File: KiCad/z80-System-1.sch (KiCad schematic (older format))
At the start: 6 parts, among them J1 FTDI Header, U1 62256, U2 Z80CPU, U3 AT28C64, U4 16550, X1 ACO-1.8432MHz

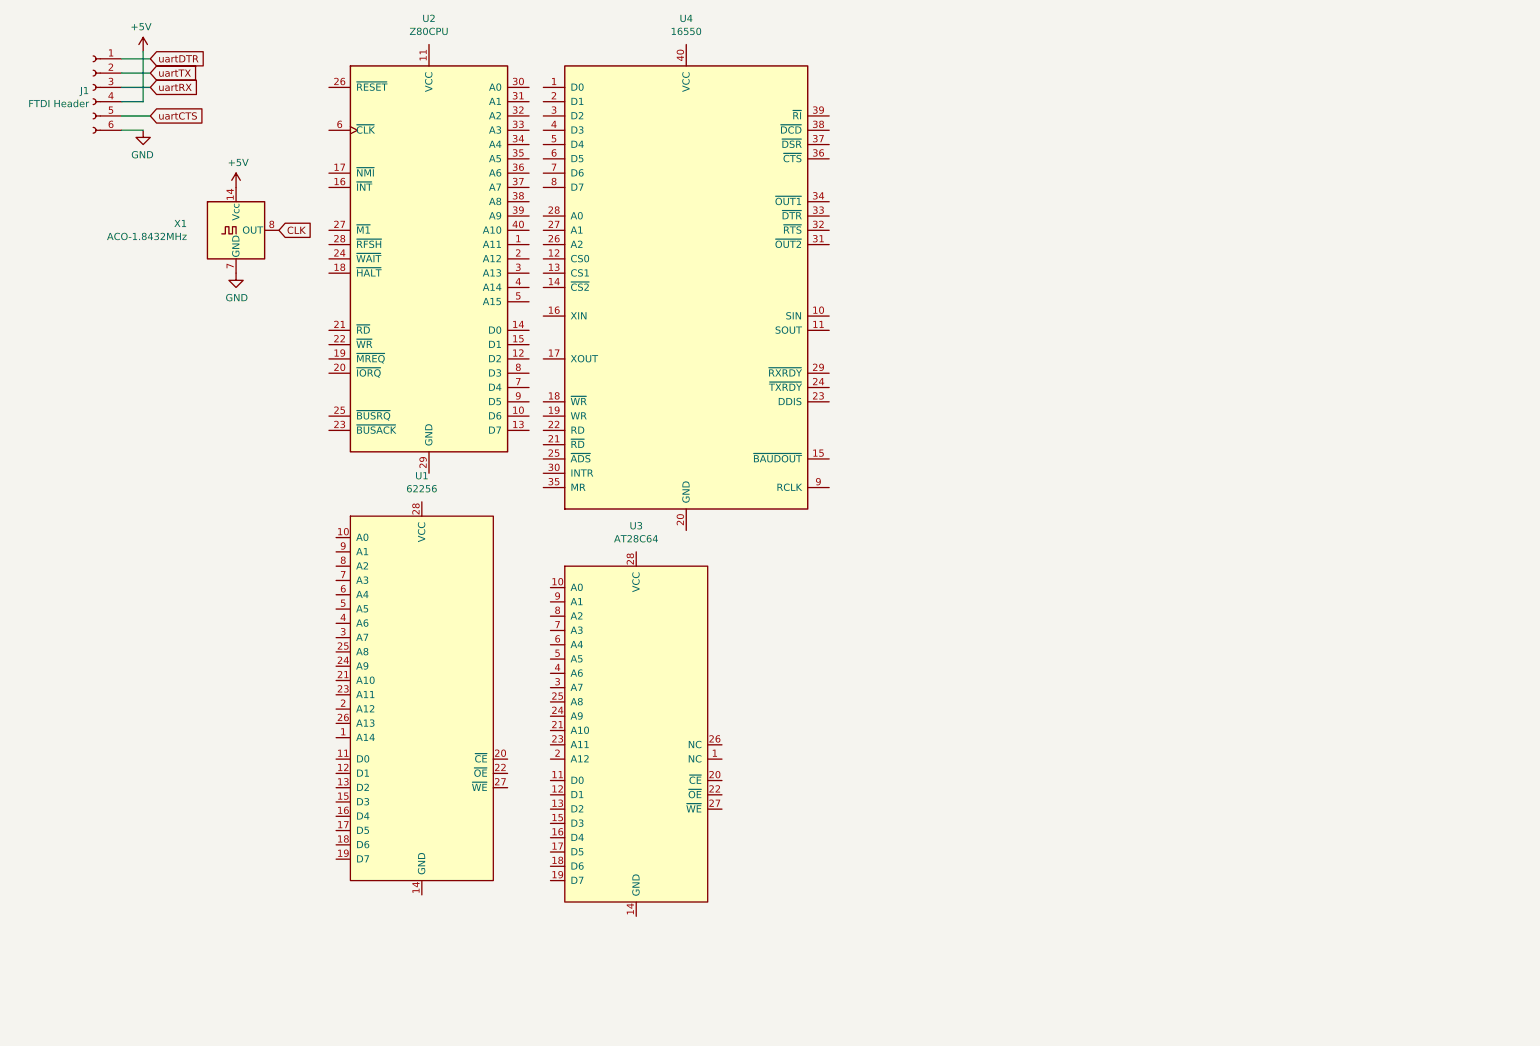
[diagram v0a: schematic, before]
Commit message: basic wiring to the cpu
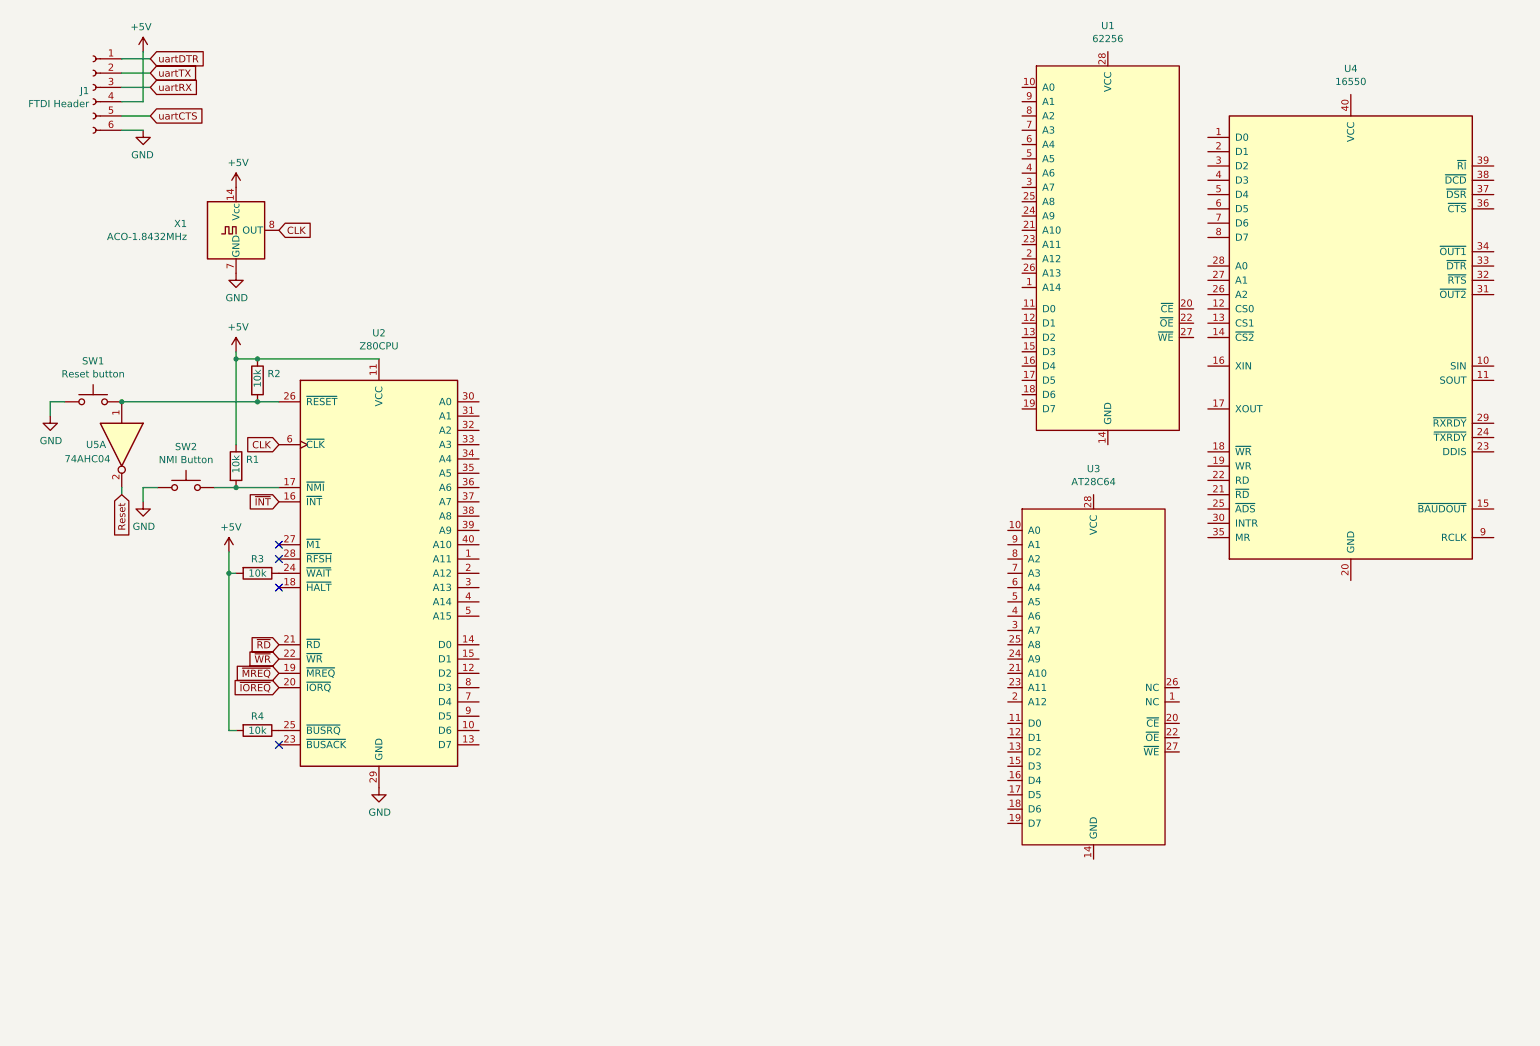
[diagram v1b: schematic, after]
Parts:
- added R1, R2, R3, R4: 10k, symbol Device:R
- added SW1: Reset button, symbol Switch:SW_Push
- added SW2: NMI Button, symbol Switch:SW_Push
- added U5: 74AHC04, symbol 74xx:74AHC04
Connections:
- net +5V: now also U2.11 (VCC), R1.1, R2.1, R3.2, R4.2
- net CLK: now also U2.6 (~CLK~)
- net GND: now also U2.29 (GND), SW1.1, SW2.1
- net ~INT: now reaches U2.16 (~INT~)
- net at U2.17 (~NMI~): now also R1.2, SW2.2
- net ~MREQ: now reaches U2.19 (~MREQ~)
- net ~IOREQ: now reaches U2.20 (~IORQ~)
- net ~RD: now reaches U2.21 (~RD~)
- net ~WR: now reaches U2.22 (~WR~)
- net at U2.24 (~WAIT~): now also R3.1
- net at U2.25 (~BUSRQ~): now also R4.1
- net at U2.26 (~RESET~): now also R2.2, SW1.2, U5.1
- new net Reset: U5.2
- no-connect marks 0 -> 4
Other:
- moved on the sheet: U1, U2, U3, U4
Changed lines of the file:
@@
 L CPU:Z80CPU U2
 U 1 1 601D54F5
-P 3350 2200
-F 0 "U2" H 3350 3881 50  0000 C CNN
-F 1 "Z80CPU" H 3350 3790 50  0000 C CNN
-F 2 "" H 3350 2600 50  0001 C CNN
-F 3 "www.zilog.com/manage_directlink.php?filepath=docs/z80/um0080" H 3350 2600 50  0001 C CNN
-	1    3350 2200
+P 3000 4400
+F 0 "U2" H 3000 6081 50  0000 C CNN
+F 1 "Z80CPU" H 3000 5990 50  0000 C CNN
+F 2 "" H 3000 4800 50  0001 C CNN
+F 3 "www.zilog.com/manage_directlink.php?filepath=docs/z80/um0080" H 3000 4800 50  0001 C CNN
+	1    3000 4400
 	1    0    0    -1
 $EndComp
@@
 L Interface_UART:16550 U4
 U 1 1 601D7ADE
-P 5150 2400
-F 0 "U4" H 5150 4281 50  0000 C CNN
-F 1 "16550" H 5150 4190 50  0000 C CNN
-F 2 "Package_DIP:DIP-40_W15.24mm" H 5150 2400 50  0001 C CIN
-F 3 "http://www.ti.com/lit/ds/symlink/pc16550d.pdf" H 5150 2400 50  0001 C CNN
-	1    5150 2400
+P 9800 2750
+F 0 "U4" H 9800 4631 50  0000 C CNN
+F 1 "16550" H 9800 4540 50  0000 C CNN
+F 2 "Package_DIP:DIP-40_W15.24mm" H 9800 2750 50  0001 C CIN
+F 3 "http://www.ti.com/lit/ds/symlink/pc16550d.pdf" H 9800 2750 50  0001 C CNN
+	1    9800 2750
 	1    0    0    -1
 $EndComp
@@
 L z80_System_1:62256 U1
 U 1 1 601C079D
-P 3300 5200
-F 0 "U1" H 3300 6681 50  0000 C CNN
-F 1 "62256" H 3300 6590 50  0000 C CNN
-F 2 "" H 850 6300 50  0001 C CNN
-F 3 "" H 850 6300 50  0001 C CNN
-	1    3300 5200
+P 8100 2050
+F 0 "U1" H 8100 3531 50  0000 C CNN
+F 1 "62256" H 8100 3440 50  0000 C CNN
+F 2 "" H 5650 3150 50  0001 C CNN
+F 3 "" H 5650 3150 50  0001 C CNN
+	1    8100 2050
 	1    0    0    -1
 $EndComp
@@
 L z80_System_1:AT28C64 U3
 U 1 1 601C1ED0
-P 4800 5450
-F 0 "U3" H 4800 6831 50  0000 C CNN
-F 1 "AT28C64" H 4800 6740 50  0000 C CNN
-F 2 "" H 4700 5450 50  0001 C CNN
-F 3 "" H 4700 5450 50  0001 C CNN
-	1    4800 5450
-	1    0    0    -1
-$EndComp
+P 8000 5050
+F 0 "U3" H 8000 6431 50  0000 C CNN
+F 1 "AT28C64" H 8000 6340 50  0000 C CNN
+F 2 "" H 7900 5050 50  0001 C CNN
+F 3 "" H 7900 5050 50  0001 C CNN
+	1    8000 5050
+	1    0    0    -1
+$EndComp
+Text GLabel 2300 3500 0    50   Input ~ 0
+CLK
+$Comp
+L Switch:SW_Push SW1
+U 1 1 601DBCFB
+P 1000 3200
+F 0 "SW1" H 1000 3485 50  0000 C CNN
+F 1 "Reset button" H 1000 3394 50  0000 C CNN
+F 2 "" H 1000 3400 50  0001 C CNN
+F 3 "~" H 1000 3400 50  0001 C CNN
+	1    1000 3200
+	1    0    0    -1
+$EndComp
+$Comp
+L power:GND #PWR05
+U 1 1 601DC395
+P 700 3300
+F 0 "#PWR05" H 700 3050 50  0001 C CNN
+F 1 "GND" H 705 3127 50  0000 C CNN
+F 2 "" H 700 3300 50  0001 C CNN
+F 3 "" H 700 3300 50  0001 C CNN
+	1    700  3300
+	1    0    0    -1
+$EndComp
+Wire Wire Line
+	800  3200 700  3200
+Wire Wire Line
+	700  3200 700  3300
+$Comp
+L 74xx:74AHC04 U5
+U 1 1 601DDEF6
+P 1200 3500
+F 0 "U5" V 1200 3250 50  0000 L CNN
+F 1 "74AHC04" V 1300 3100 50  0000 L CNN
+F 2 "" H 1200 3500 50  0001 C CNN
+F 3 "https://assets.nexperia.com/documents/data-sheet/74AHC_AHCT04.pdf" H 1200 3500 50  0001 C CNN
+	1    1200 3500
+	0    1    1    0
+$EndComp
+$Comp
+L Device:R R1
+U 1 1 601EE768
+P 2000 3650
+F 0 "R1" H 2070 3696 50  0000 L CNN
+F 1 "10k" V 2000 3600 50  0000 L CNN
+F 2 "" V 1930 3650 50  0001 C CNN
+F 3 "~" H 2000 3650 50  0001 C CNN
+	1    2000 3650
+	1    0    0    -1
+$EndComp
+Wire Wire Line
+	3000 2900 2150 2900
+Wire Wire Line
+	2300 3200 2150 3200
+Wire Wire Line
+	2000 3500 2000 2900
+Wire Wire Line
+	2000 2900 2150 2900
+Connection ~ 2150 2900
+Connection ~ 2150 3200
+$Comp
+L power:+5V #PWR07
+U 1 1 601F1F71
+P 1950 4250
+F 0 "#PWR07" H 1950 4100 50  0001 C CNN
+F 1 "+5V" H 1965 4423 50  0000 C CNN
+F 2 "" H 1950 4250 50  0001 C CNN
+F 3 "" H 1950 4250 50  0001 C CNN
+	1    1950 4250
+	1    0    0    -1
+$EndComp
+Wire Wire Line
+	2000 2850 2000 2900
+Connection ~ 2000 2900
+Wire Wire Line
+	2300 3800 2000 3800
+$Comp
+L Switch:SW_Push SW2
+U 1 1 601F323F
+P 1650 3800
+F 0 "SW2" H 1650 4085 50  0000 C CNN
+F 1 "NMI Button" H 1650 3994 50  0000 C CNN
+F 2 "" H 1650 4000 50  0001 C CNN
+F 3 "~" H 1650 4000 50  0001 C CNN
+	1    1650 3800
+	1    0    0    -1
+$EndComp
+$Comp
+L power:GND #PWR06
+U 1 1 601F4A44
+P 1350 3900
+F 0 "#PWR06" H 1350 3650 50  0001 C CNN
+F 1 "GND" H 1355 3727 50  0000 C CNN
+F 2 "" H 1350 3900 50  0001 C CNN
+F 3 "" H 1350 3900 50  0001 C CNN
+	1    1350 3900
+	1    0    0    -1
+$EndComp
+Wire Wire Line
+	2000 3800 1850 3800
+Connection ~ 2000 3800
+Wire Wire Line
+	1450 3800 1350 3800
+Wire Wire Line
+	1350 3800 1350 3900
+$Comp
+L Device:R R2
+U 1 1 601F64CB
+P 2150 3050
+F 0 "R2" H 2220 3096 50  0000 L CNN
+F 1 "10k" V 2150 3000 50  0000 L CNN
+F 2 "" V 2080 3050 50  0001 C CNN
+F 3 "~" H 2150 3050 50  0001 C CNN
+	1    2150 3050
+	1    0    0    -1
+$EndComp
+Text GLabel 2300 3900 0    50   Input ~ 0
+~INT
+NoConn ~ 2300 4200
+NoConn ~ 2300 4300
+$Comp
+L Device:R R3
+U 1 1 601F88BB
+P 2150 4400
+F 0 "R3" V 2050 4400 50  0000 C CNN
+F 1 "10k" V 2150 4400 50  0000 C CNN
+F 2 "" V 2080 4400 50  0001 C CNN
+F 3 "~" H 2150 4400 50  0001 C CNN
+	1    2150 4400
+	0    1    1    0
+$EndComp
+NoConn ~ 2300 4500
+Text GLabel 2300 4900 0    50   Input ~ 0
+~RD
+Text GLabel 2300 5000 0    50   Input ~ 0
+~WR
+Text GLabel 2300 5100 0    50   Input ~ 0
+~MREQ
+Text GLabel 2300 5200 0    50   Input ~ 0
+~IOREQ
+$Comp
+L Device:R R4
+U 1 1 601FB3B2
+P 2150 5500
+F 0 "R4" V 2050 5500 50  0000 C CNN
+F 1 "10k" V 2150 5500 50  0000 C CNN
+F 2 "" V 2080 5500 50  0001 C CNN
+F 3 "~" H 2150 5500 50  0001 C CNN
+	1    2150 5500
+	0    1    1    0
+$EndComp
+NoConn ~ 2300 5600
+Wire Wire Line
+	2000 4400 1950 4400
+Wire Wire Line
+	1950 4400 1950 4250
+Wire Wire Line
+	1950 4400 1950 5500
+Wire Wire Line
+	1950 5500 2000 5500
+Connection ~ 1950 4400
+$Comp
+L power:+5V #PWR08
+U 1 1 601FD472
+P 2000 2850
+F 0 "#PWR08" H 2000 2700 50  0001 C CNN
+F 1 "+5V" H 2015 3023 50  0000 C CNN
+F 2 "" H 2000 2850 50  0001 C CNN
+F 3 "" H 2000 2850 50  0001 C CNN
+	1    2000 2850
+	1    0    0    -1
+$EndComp
+Wire Wire Line
+	1200 3200 2150 3200
+Connection ~ 1200 3200
+Text GLabel 1200 3850 3    50   Input ~ 0
+Reset
+Wire Wire Line
+	1200 3800 1200 3850
+$Comp
+L power:GND #PWR?
+U 1 1 60212DC5
+P 3000 5900
+F 0 "#PWR?" H 3000 5650 50  0001 C CNN
+F 1 "GND" H 3005 5727 50  0000 C CNN
+F 2 "" H 3000 5900 50  0001 C CNN
+F 3 "" H 3000 5900 50  0001 C CNN
+	1    3000 5900
+	1    0    0    -1
+$EndComp

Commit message: Finished schematic and created simple board layout
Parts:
- removed U5: 74AHC04, symbol 74xx:74AHC04
- added C1, C2, C3, C4, C5, C6: 100nF, Capacitor_THT:C_Disc_D7.0mm_W2.5mm_P5.00mm, symbol Device:C
- added R5, R6: 10k, Resistor_THT:R_Axial_DIN0204_L3.6mm_D1.6mm_P5.08mm_Horizontal, symbol Device:R
- added U5: 74LS04, symbol 74xx:74LS04
- added U6: 74LS32, symbol 74xx:74LS32
- J1: footprint (none) -> Connector_PinSocket_2.54mm:PinSocket_1x06_P2.54mm_Vertical
- R1, R2, R3, R4: footprint (none) -> Resistor_THT:R_Axial_DIN0204_L3.6mm_D1.6mm_P5.08mm_Horizontal
- SW1, SW2: footprint (none) -> Button_Switch_THT:SW_PUSH_6mm
- U1, U3: footprint (none) -> Package_DIP:DIP-28_W15.24mm
- U2: footprint (none) -> Package_DIP:DIP-40_W15.24mm
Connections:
- net +5V: now also U1.28 (VCC), U3.28 (VCC), U4.40 (VCC), C1.1, C2.1, C3.1, C4.1, C5.1, C6.1, R5.2, R6.2, U5.14 (VCC), U6.14 (VCC)
- net CLK: now also U4.16 (XIN)
- net GND: now also U1.14 (GND), U3.14 (GND), U4.19 (WR), U4.20 (GND), U4.22 (RD), U4.25 (~ADS~), C1.2, C2.2, C3.2, C4.2, C5.2, C6.2, U5.7 (GND), U6.7 (GND)
- net Reset: now also U4.35 (MR), U5.2
- net uartCTS: now also U4.36 (~CTS~)
- net uartDTR: now also U4.33 (~DTR~)
- net ~INT: now also U5.6
- net ~MREQ: now also U6.1, U6.4
- net ~RD: now also U1.22 (~OE), U3.22 (~OE), U4.21 (~RD~)
- net ~WR: now also U1.27 (~WE), U4.18 (~WR~)
- net A14: now reaches U1.1 (A14)
- net A14: now also U2.4 (A14)
- net A0: now reaches U1.10 (A0)
- net A0: now also U2.30 (A0), U3.10 (A0), U4.28 (A0)
- net D0: now reaches U1.11 (D0)
- net D0: now also U2.14 (D0), U3.11 (D0), U4.1 (D0)
- net D1: now reaches U1.12 (D1)
- net D1: now also U2.15 (D1), U3.12 (D1), U4.2 (D1)
- net D2: now reaches U1.13 (D2)
- net D2: now also U2.12 (D2), U3.13 (D2), U4.3 (D2)
- net D3: now reaches U1.15 (D3)
- net D3: now also U2.8 (D3), U3.15 (D3), U4.4 (D3)
- net D4: now reaches U1.16 (D4)
- net D4: now also U2.7 (D4), U3.16 (D4), U4.5 (D4)
- net D5: now reaches U1.17 (D5)
- net D5: now also U2.9 (D5), U3.17 (D5), U4.6 (D5)
- net D6: now reaches U1.18 (D6)
- net D6: now also U2.10 (D6), U3.18 (D6), U4.7 (D6)
- net D7: now reaches U1.19 (D7)
- net D7: now also U2.13 (D7), U3.19 (D7), U4.8 (D7)
- net A12: now reaches U1.2 (A12)
- net A12: now also U2.2 (A12), U3.2 (A12)
- net ~CE_RAM: now reaches U1.20 (~CE)
- net ~CE_RAM: now also U6.3
- net A10: now reaches U1.21 (A10)
- net A10: now also U2.40 (A10), U3.21 (A10)
- net A11: now reaches U1.23 (A11)
- net A11: now also U2.1 (A11), U3.23 (A11)
- net A9: now reaches U1.24 (A9)
- net A9: now also U2.39 (A9), U3.24 (A9)
- net A8: now reaches U1.25 (A8)
- net A8: now also U2.38 (A8), U3.25 (A8)
- net A13: now reaches U1.26 (A13)
- net A13: now also U2.3 (A13)
- net A7: now reaches U1.3 (A7)
- net A7: now also U2.37 (A7), U3.3 (A7)
- net A6: now reaches U1.4 (A6)
- net A6: now also U2.36 (A6), U3.4 (A6)
- net A5: now reaches U1.5 (A5)
- net A5: now also U2.35 (A5), U3.5 (A5)
- net A4: now reaches U1.6 (A4)
- net A4: now also U2.34 (A4), U3.6 (A4)
- net A3: now reaches U1.7 (A3)
- net A3: now also U2.33 (A3), U3.7 (A3)
- net A2: now reaches U1.8 (A2)
- net A2: now also U2.32 (A2), U3.8 (A2), U4.26 (A2)
- net A1: now reaches U1.9 (A1)
- net A1: now also U2.31 (A1), U3.9 (A1), U4.27 (A1)
- net ~CE_ROM: now reaches U3.20 (~CE)
- net ~CE_ROM: now also U6.6
- net at R2.2, SW1.2, U2.26 (~RESET~): now also U5.1
- net A15: now reaches U2.5 (A15)
- net A15: now also U5.3, U6.5
- net RX: now reaches U4.10 (SIN)
- net TX: now reaches U4.11 (SOUT)
- net at U4.12 (CS0): now also R5.1
- net at U4.13 (CS1): now also R6.1
- net ~IORQ: now reaches U4.14 (~CS2~)
- net at U4.15 (~BAUDOUT~): now also U4.9 (RCLK)
- net at U4.30 (INTR): now also U5.5
- new net: U5.4, U6.2
- no-connect marks 4 -> 17
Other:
- moved on the sheet: U1, U3, U4

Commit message: Layout 1 finished
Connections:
- net RX is gone; now on net uartRX: U4.10 (SIN)
- net TX is gone; now on net uartTX: U4.11 (SOUT)
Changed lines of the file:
@@
 NoConn ~ 8850 3650
 Text GLabel 8850 3250 2    50   Input ~ 0
-RX
+uartRX
 Text GLabel 8850 3350 2    50   Input ~ 0
-TX
+uartTX
 Text GLabel 8850 2150 2    50   Input ~ 0
 uartCTS
@@
 Wire Wire Line
 	10150 1150 10600 1150
-Wire Bus Line
-	6700 950  6700 2650
-Wire Bus Line
-	3850 950  3850 7050
 $Comp
 L 74xx:74LS04 U5
@@
 	1    0    0    -1
 $EndComp
+Wire Bus Line
+	6700 950  6700 2650
+Wire Bus Line
+	3850 950  3850 7050
 $EndSCHEMATC
